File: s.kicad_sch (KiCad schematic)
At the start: 17 parts, among them J1 USB4085-GF-A_REVB, J2 UART connector, J5 SW_3v3, SW26 210-4MS, U1 ESP32-S3-WROOM-1, U2 MCP1825S

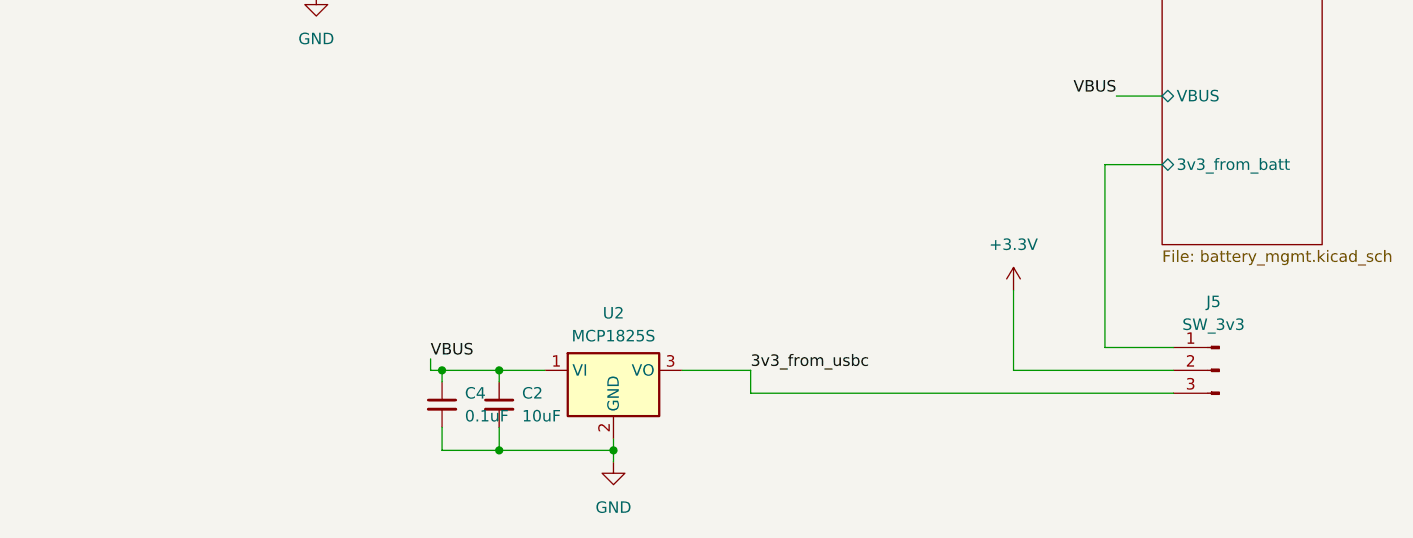
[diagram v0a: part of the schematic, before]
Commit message: use 0-ohm resistors, not switches, to control power source
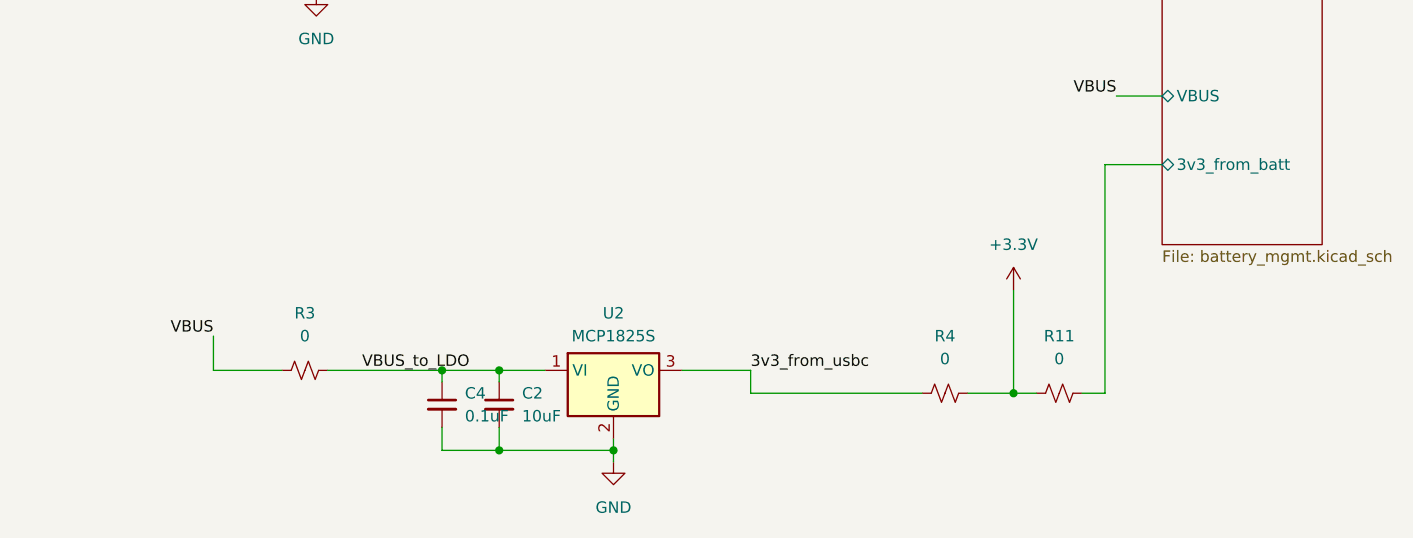
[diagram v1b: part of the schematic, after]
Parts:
- removed J5: SW_3v3, Connector_PinHeader_2.54mm:PinHeader_1x03_P2.54mm_Vertical, symbol Connector:Conn_01x03_Pin
- added R11, R3, R4: 0, Resistor_SMD:R_0805_2012Metric_Pad1.20x1.40mm_HandSolder, symbol Device:R_Small_US
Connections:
- net +3.3V: now also R11.1, R4.2
- net 3v3_from_usbc: now also R4.1
- net VBUS: now also R3.1; no longer C2.1, C4.1, U2.1 (VI)
- net battery_mgmt/3v3_from_batt: now also R11.2
- new net VBUS_to_LDO: C2.1, C4.1, R3.2, U2.1 (VI)

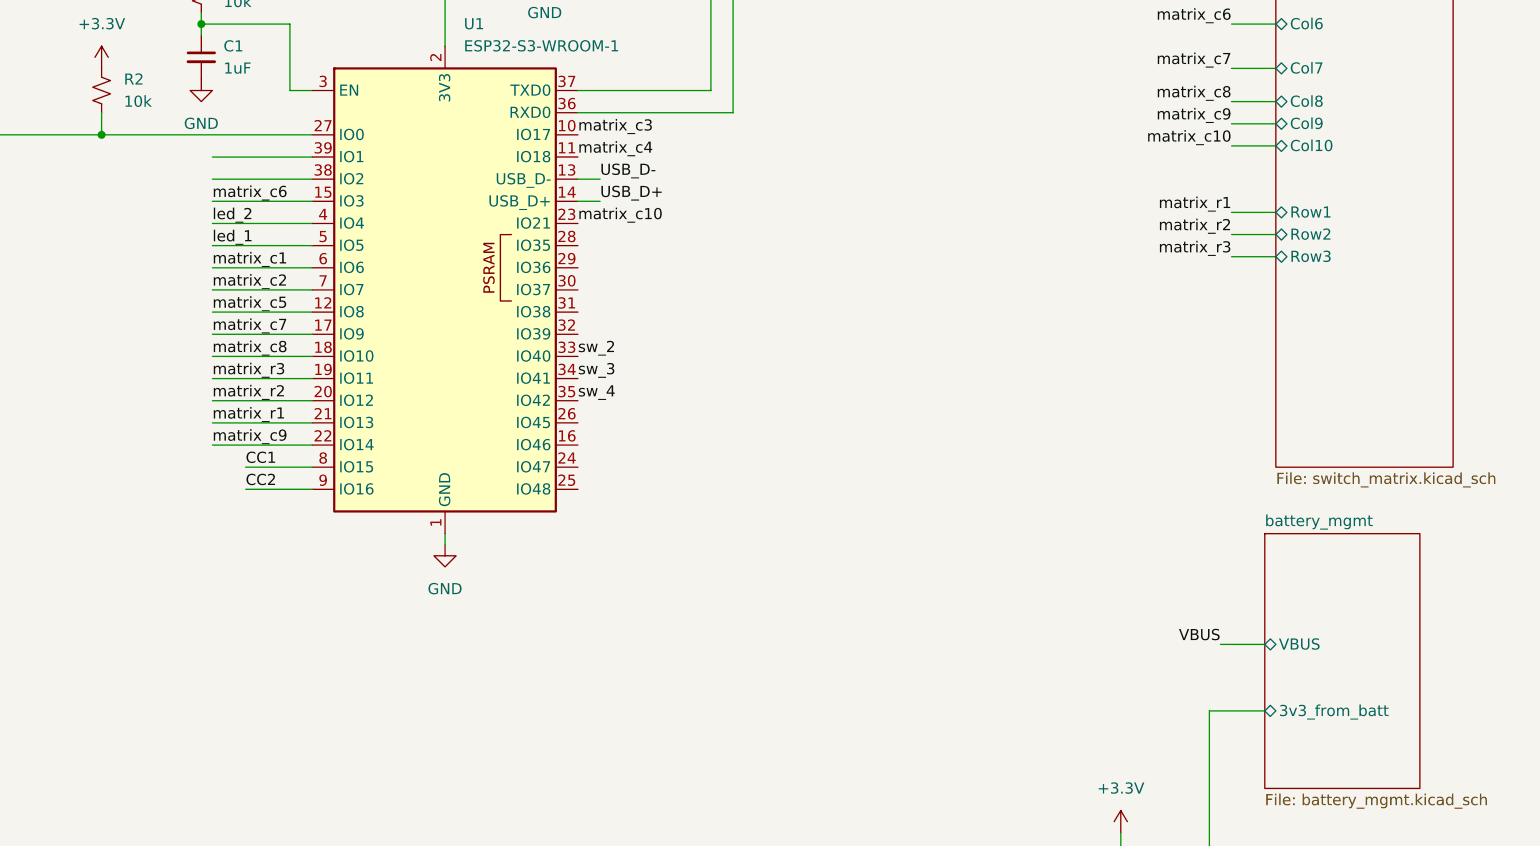
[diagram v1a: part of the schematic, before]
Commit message: add a voltage divider for battery voltage monitoring
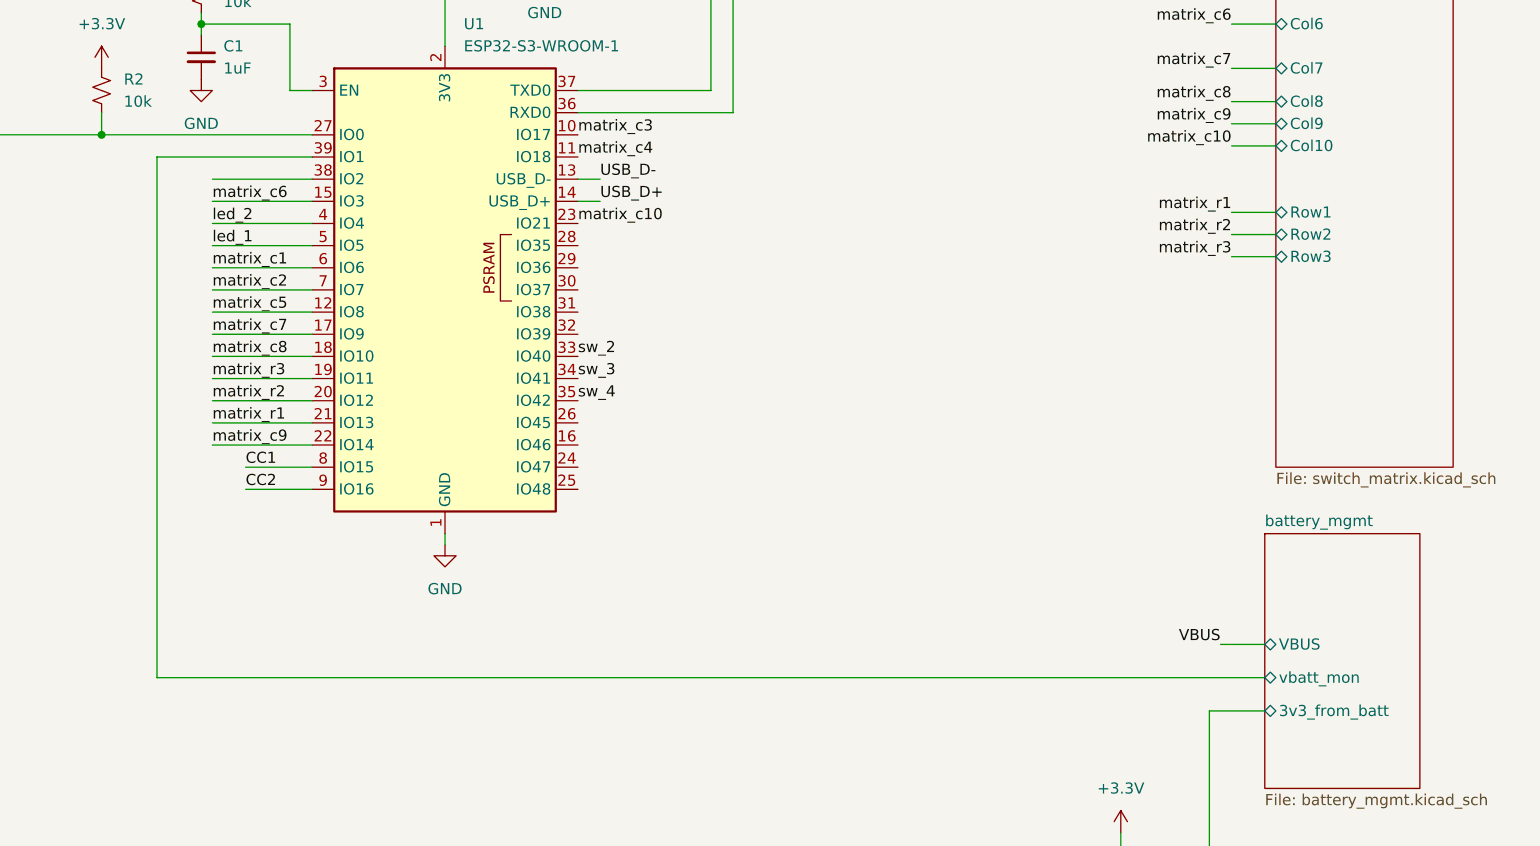
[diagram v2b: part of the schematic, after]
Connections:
- net battery_mgmt/vbatt_mon: now reaches U1.39 (IO1)
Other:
- sheet battery_mgmt ports: added vbatt_mon; removed none
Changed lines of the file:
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@@
 	(wire
 		(pts
+			(xy 128.27 58.42) (xy 146.05 58.42)
+		)
+		(stroke
+			(width 0)
+			(type default)
+		)
+	)
+	(wire
+		(pts
 			(xy 134.62 68.58) (xy 146.05 68.58)
 		)
@@
 	(wire
 		(pts
+			(xy 128.27 118.11) (xy 128.27 58.42)
+		)
+		(stroke
+			(width 0)
+			(type default)
+		)
+	)
+	(wire
+		(pts
 			(xy 134.62 60.96) (xy 146.05 60.96)
 		)
@@
 	(wire
 		(pts
-			(xy 134.62 58.42) (xy 146.05 58.42)
-		)
-		(stroke
-			(width 0)
-			(type default)
-		)
-	)
-	(wire
-		(pts
 			(xy 138.43 96.52) (xy 146.05 96.52)
 		)
@@
 	(wire
 		(pts
+			(xy 128.27 118.11) (xy 255.27 118.11)
+		)
+		(stroke
+			(width 0)
+			(type default)
+		)
+	)
+	(wire
+		(pts
 			(xy 201.93 144.78) (xy 209.55 144.78)
 		)
@@
 			(effects
 				(font
+					(size 1.27 1.27)
+				)
+				(justify left)
+			)
+		)
+		(pin "vbatt_mon" bidirectional
+			(at 255.27 118.11 180)
+			(effects
+				(font

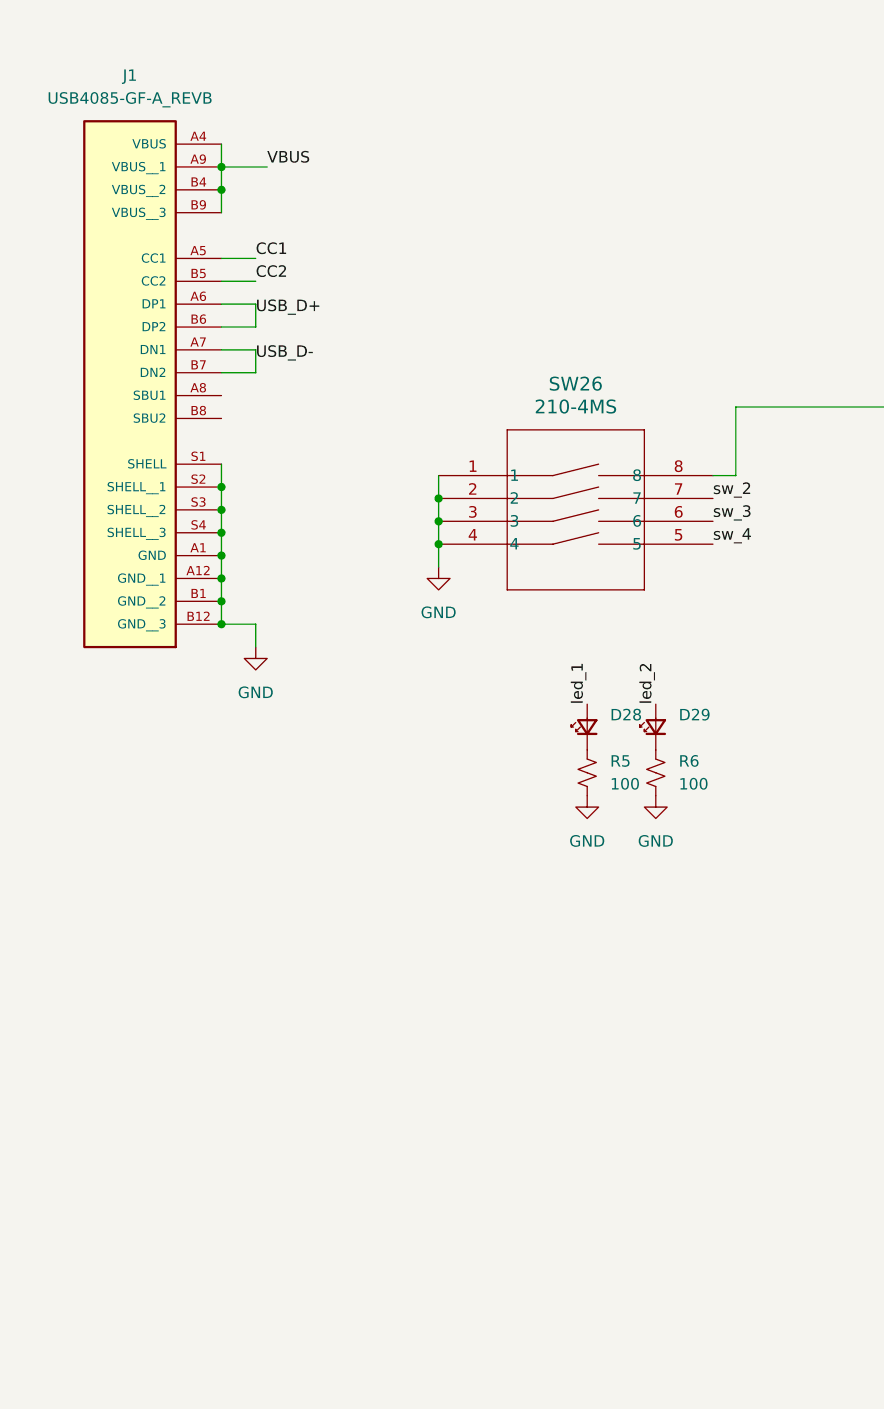
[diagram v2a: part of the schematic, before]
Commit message: new usb port footprint
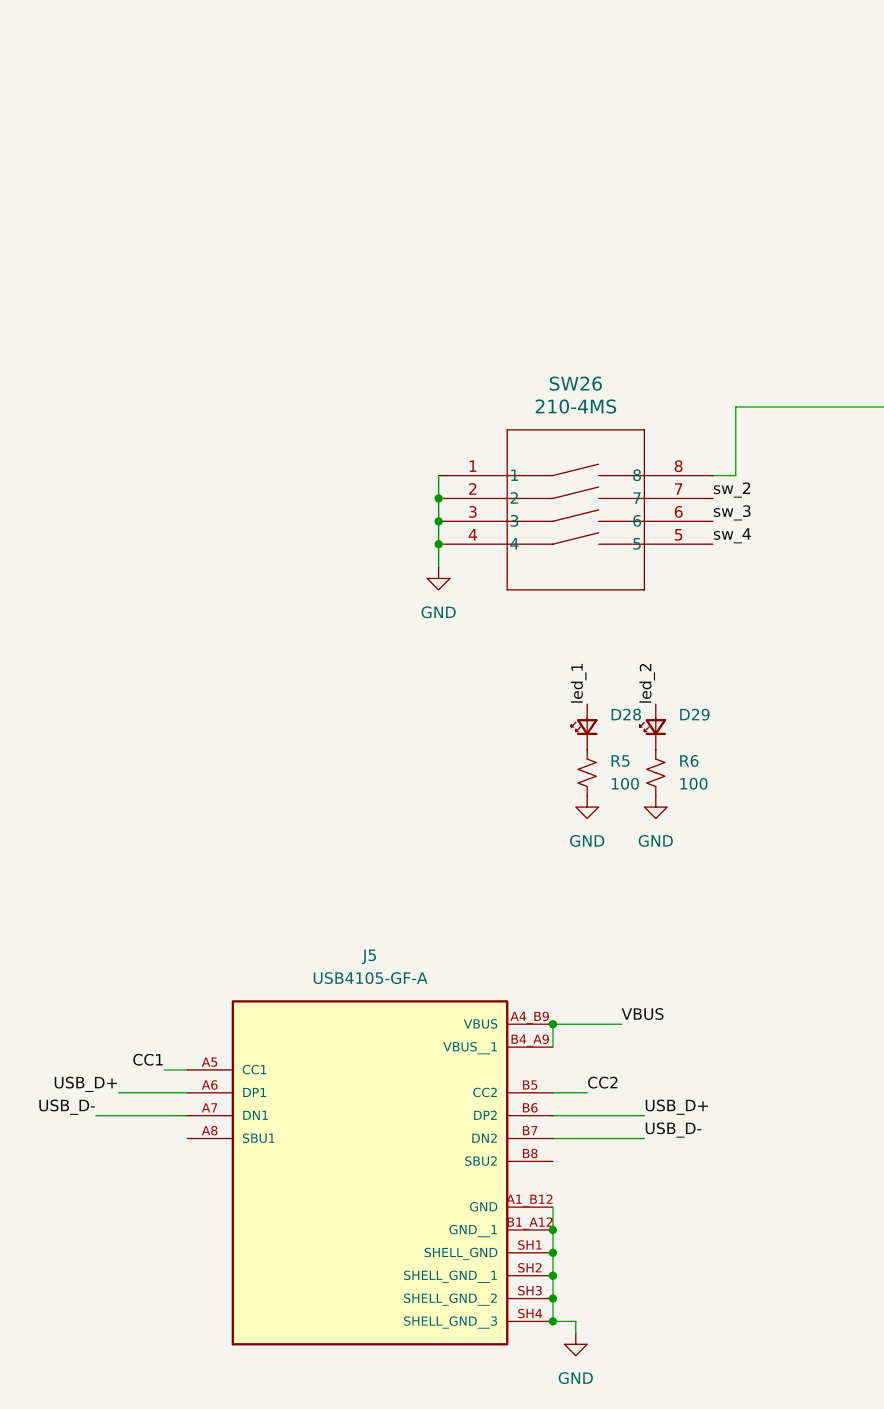
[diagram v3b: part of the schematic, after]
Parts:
- removed J1: USB4085-GF-A_REVB, USB4085_GF_A:GCT_USB4085-GF-A_REVB, symbol USB4085-GF-A_REVB:USB4085-GF-A_REVB
- added J5: USB4105-GF-A, USB4105:GCT_USB4105-GF-A, symbol USB4105-GF-A:USB4105-GF-A
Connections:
- net CC1: now also J5.A5 (CC1)
- net CC2: now also J5.B5 (CC2)
- net GND: now also J5.A1_B12 (GND), J5.B1_A12 (GND__1), J5.SH1 (SHELL_GND), J5.SH2 (SHELL_GND__1), J5.SH3 (SHELL_GND__2), J5.SH4 (SHELL_GND__3)
- net USB_D+: now also J5.A6 (DP1), J5.B6 (DP2)
- net USB_D-: now also J5.A7 (DN1), J5.B7 (DN2)
- net VBUS: now also J5.A4_B9 (VBUS), J5.B4_A9 (VBUS__1)

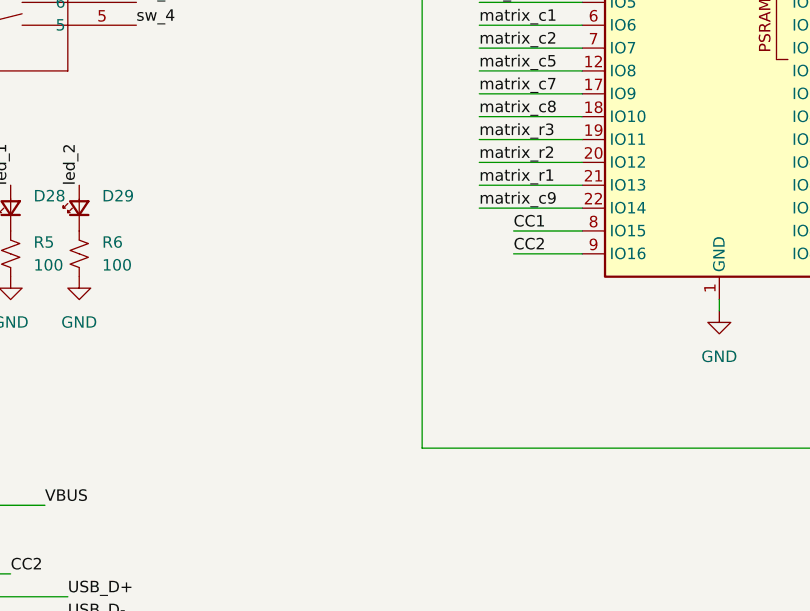
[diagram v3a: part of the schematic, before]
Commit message: reroute board
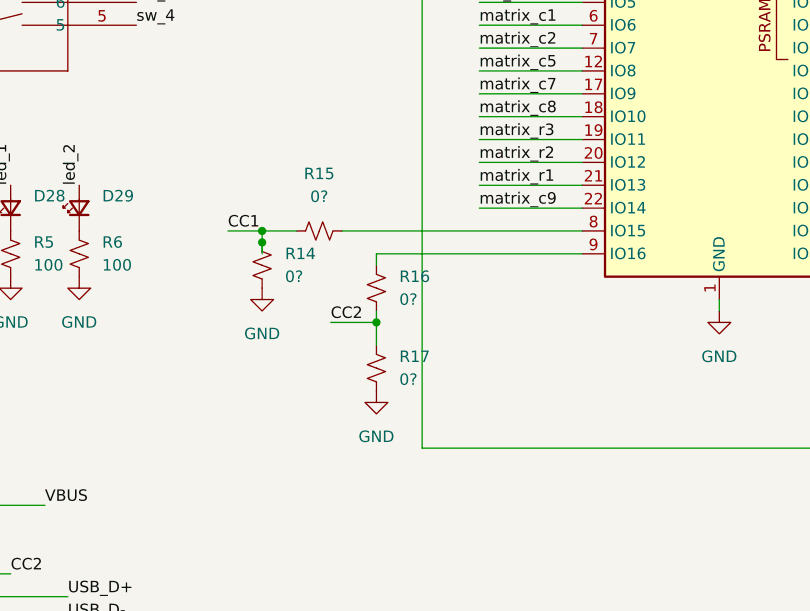
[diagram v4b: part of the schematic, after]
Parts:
- added R14, R15, R16, R17: 0?, Resistor_SMD:R_0805_2012Metric_Pad1.20x1.40mm_HandSolder, symbol Device:R_Small_US
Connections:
- net CC1: now also R14.1, R15.1; no longer U1.8 (IO15)
- net CC2: now also R16.1, R17.1; no longer U1.9 (IO16)
- net GND: now also R14.2, R17.2
- new net: R15.2, U1.8 (IO15)
- new net: R16.2, U1.9 (IO16)

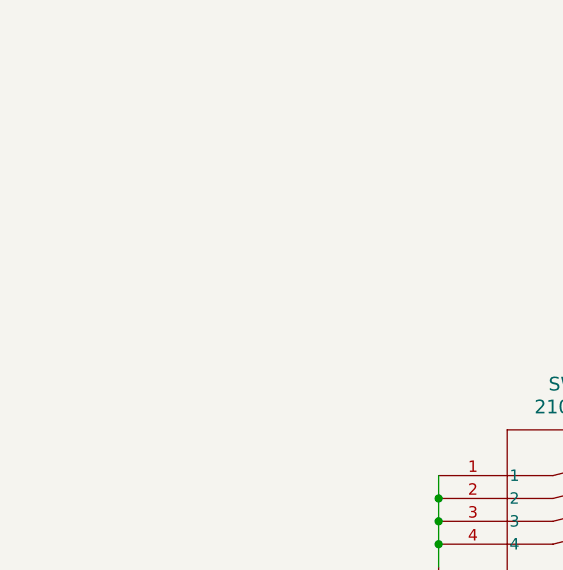
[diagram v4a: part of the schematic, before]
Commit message: add 3 of 4 mounting holes
still need to think about the last one...
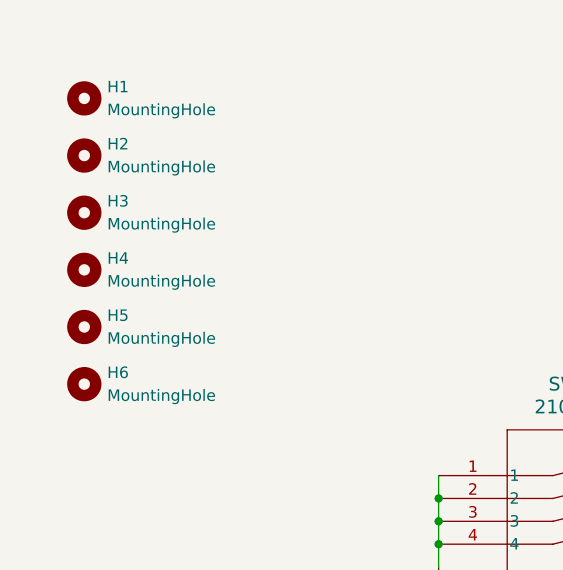
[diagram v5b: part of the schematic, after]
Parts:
- added H1, H2, H3, H4, H5, H6: MountingHole, MountingHole:MountingHole_3mm, symbol Mechanical:MountingHole
